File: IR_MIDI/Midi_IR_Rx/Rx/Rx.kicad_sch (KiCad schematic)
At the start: 34 parts, among them J1 Power In, J2 DIN-5, Q1 BPX38, Q2 2N3904, Q3 2N3904, Q4 2N3904, Q5 2N3904, Q6 2N3904, U1 4046

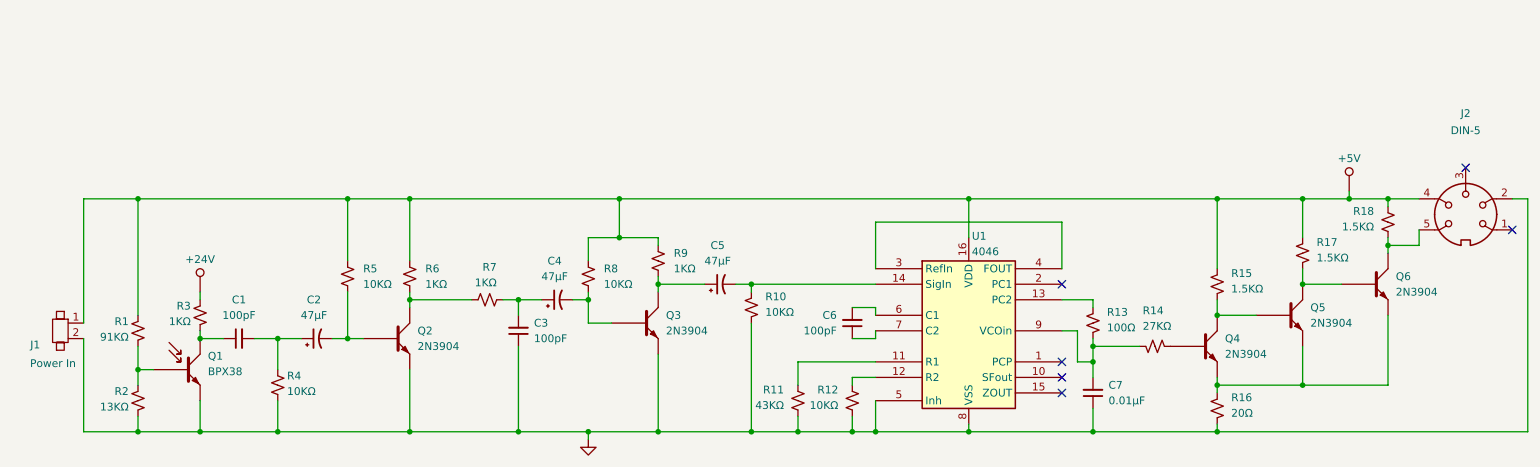
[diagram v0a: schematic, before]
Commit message: updated file structures and refreshed MIDI circuits
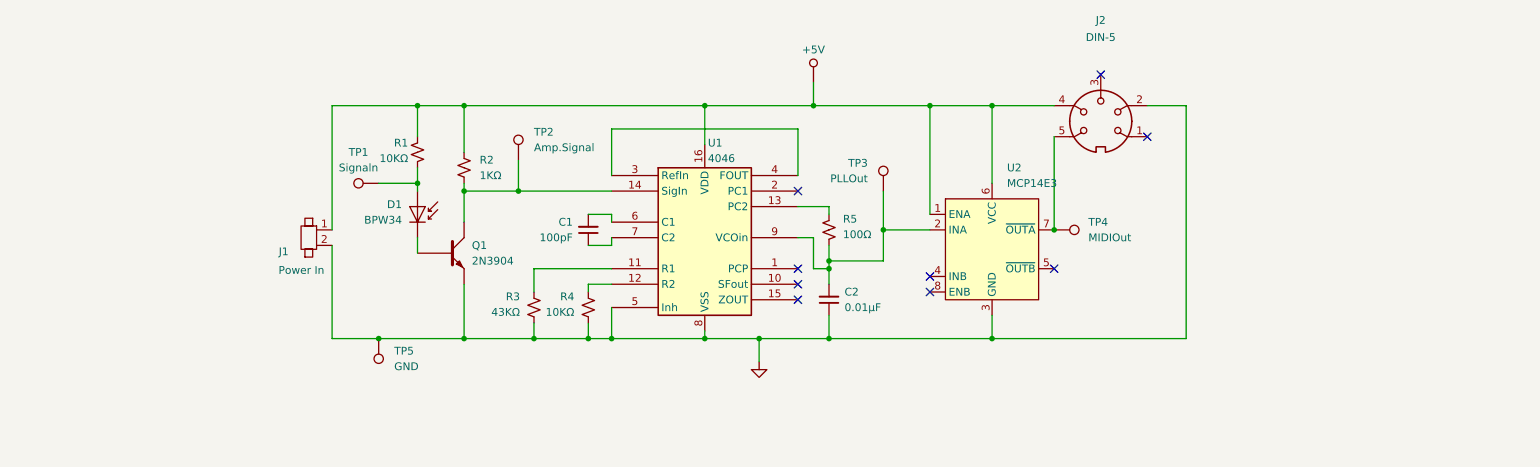
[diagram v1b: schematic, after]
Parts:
- removed C1, C3: 100pF, symbol Device:C_Small
- removed C2, C4, C5: 47µF, symbol Device:C_Polarized_Small_US
- removed Q1: BPX38, Package_TO_SOT_THT:TO-92_Inline, symbol Transistor_BJT:2N3904
- removed Q3, Q4, Q5, Q6: 2N3904, Package_TO_SOT_THT:TO-92_Inline, symbol Transistor_BJT:2N3904
- removed R1: 91KΩ, symbol Device:R_Small_US
- removed R10, R4, R5, R8: 10KΩ, symbol Device:R_Small_US
- removed R14: 27KΩ, symbol Device:R_Small_US
- removed R15, R17, R18: 1.5KΩ, symbol Device:R_Small_US
- removed R16: 20Ω, symbol Device:R_Small_US
- removed R2: 13KΩ, symbol Device:R_Small_US
- removed R7, R9: 1KΩ, symbol Device:R_Small_US
- added D1: BPW34, OptoDevice:Osram_DIL2_4.3x4.65mm_P5.08mm, symbol Sensor_Optical:BPW34
- added TP1: Signaln, symbol Connector:TestPoint
- added TP2: Amp.Signal, symbol Connector:TestPoint
- added TP3: PLLOut, symbol Connector:TestPoint
- added TP4: MIDIOut, symbol Connector:TestPoint
- added TP5: GND, symbol Connector:TestPoint
- added U2: MCP14E3, symbol 2_JB_Custom_sym:MCP14E3
- C1: renamed from C6; footprint (none) -> 2JB_Footprints:C_0805
- C2: renamed from C7; footprint (none) -> 2JB_Footprints:C_0805
- J1: footprint (none) -> 2JB_Footprints:RCA Jack P177
- J2: footprint (none) -> 2JB_Footprints:DIN-5PIN_MIDI
- R1: renamed from R3; value 1KΩ -> 10KΩ; footprint (none) -> 2JB_Footprints:C_0805
- R2: renamed from R6; footprint (none) -> 2JB_Footprints:C_0805
- R3: renamed from R11; footprint (none) -> 2JB_Footprints:C_0805
- R4: renamed from R12; footprint (none) -> 2JB_Footprints:C_0805
- R5: renamed from R13; footprint (none) -> 2JB_Footprints:C_0805
- U1: footprint (none) -> Package_SO:SOP-16_4.4x10.4mm_P1.27mm
- renumbered Q2 to Q1
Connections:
- net GND: now also TP5.1, U2.3 (GND)
- net at R1.1: now also D1.2 (A), TP1.1
- net at J1.1, J2.4, R2.2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: now also R1.2, U2.1 (ENA), U2.6 (VCC)
- net at Q1.3 (C), R2.1: now also U1.14 (SigIn), TP2.1
- net at C2.2, R5.2, U1.9 (VCOin): now also TP3.1, U2.2 (INA)
- net at Q1.2 (B): now also D1.1 (K)
- net at J2.5: now also TP4.1, U2.7 (~{OUTA})
- no-connect marks 6 -> 9
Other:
- moved on the sheet: C1, C2, J1, J2, Q1, R1, R2, R3, R4, R5, U1
